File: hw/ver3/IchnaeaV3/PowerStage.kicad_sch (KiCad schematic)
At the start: 68 parts, among them Q1 BSS138, U2 LTC7871, U3 AP66200FVBW-13, U4 LM1117MP-5.0

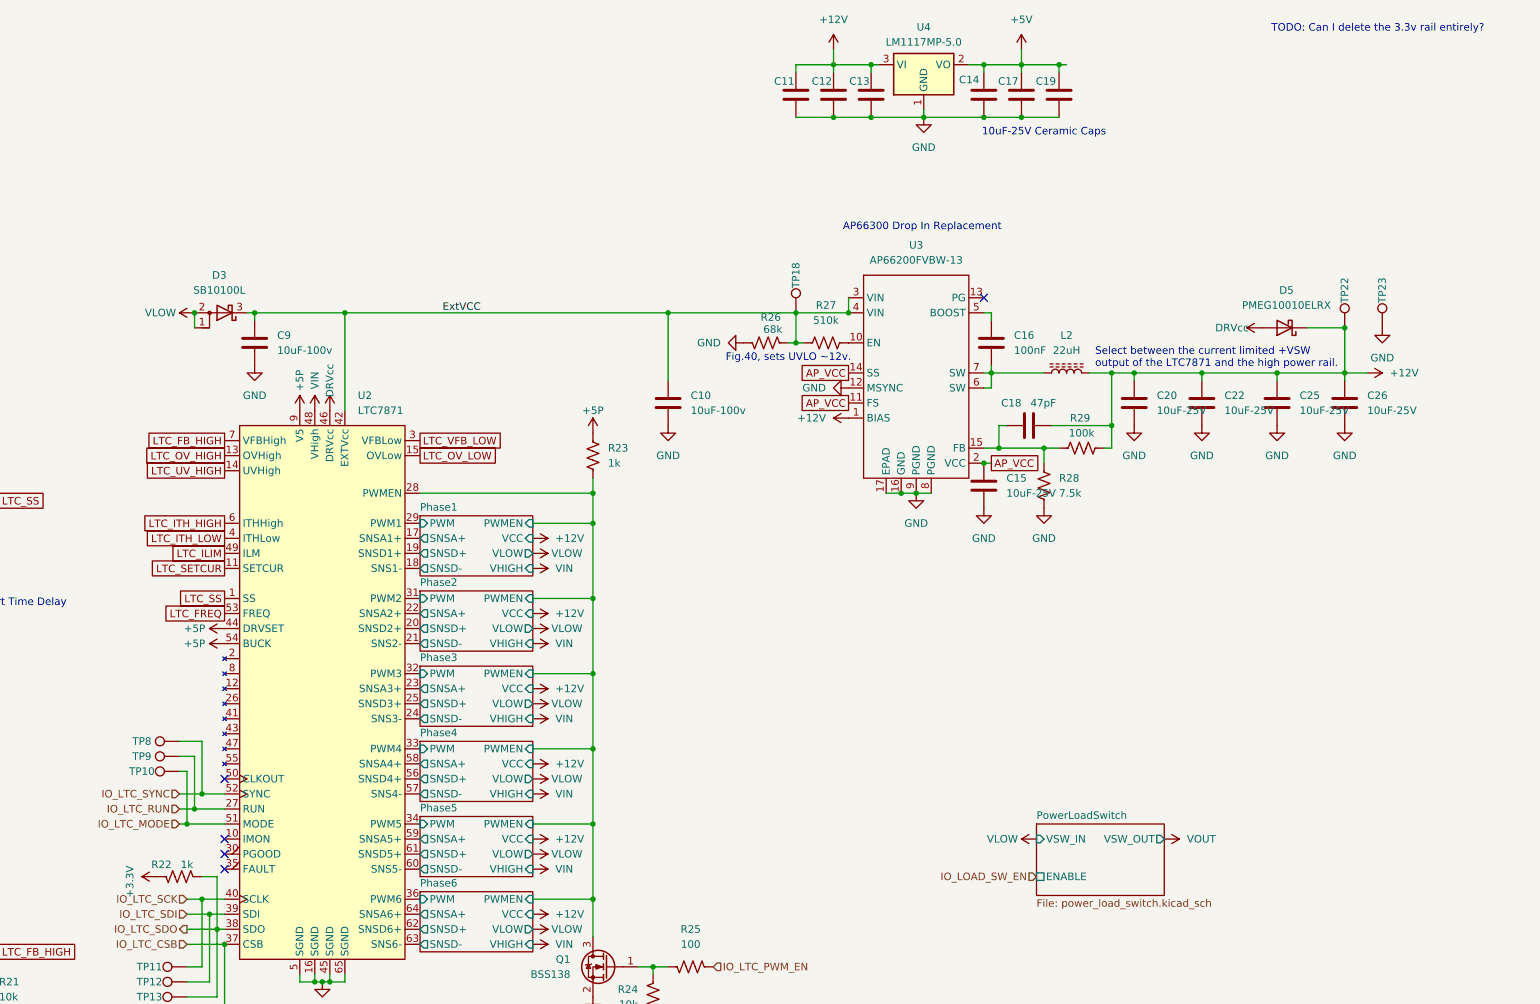
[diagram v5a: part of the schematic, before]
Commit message: Start rework of power stage layout to shorten inductive path and increase current handling
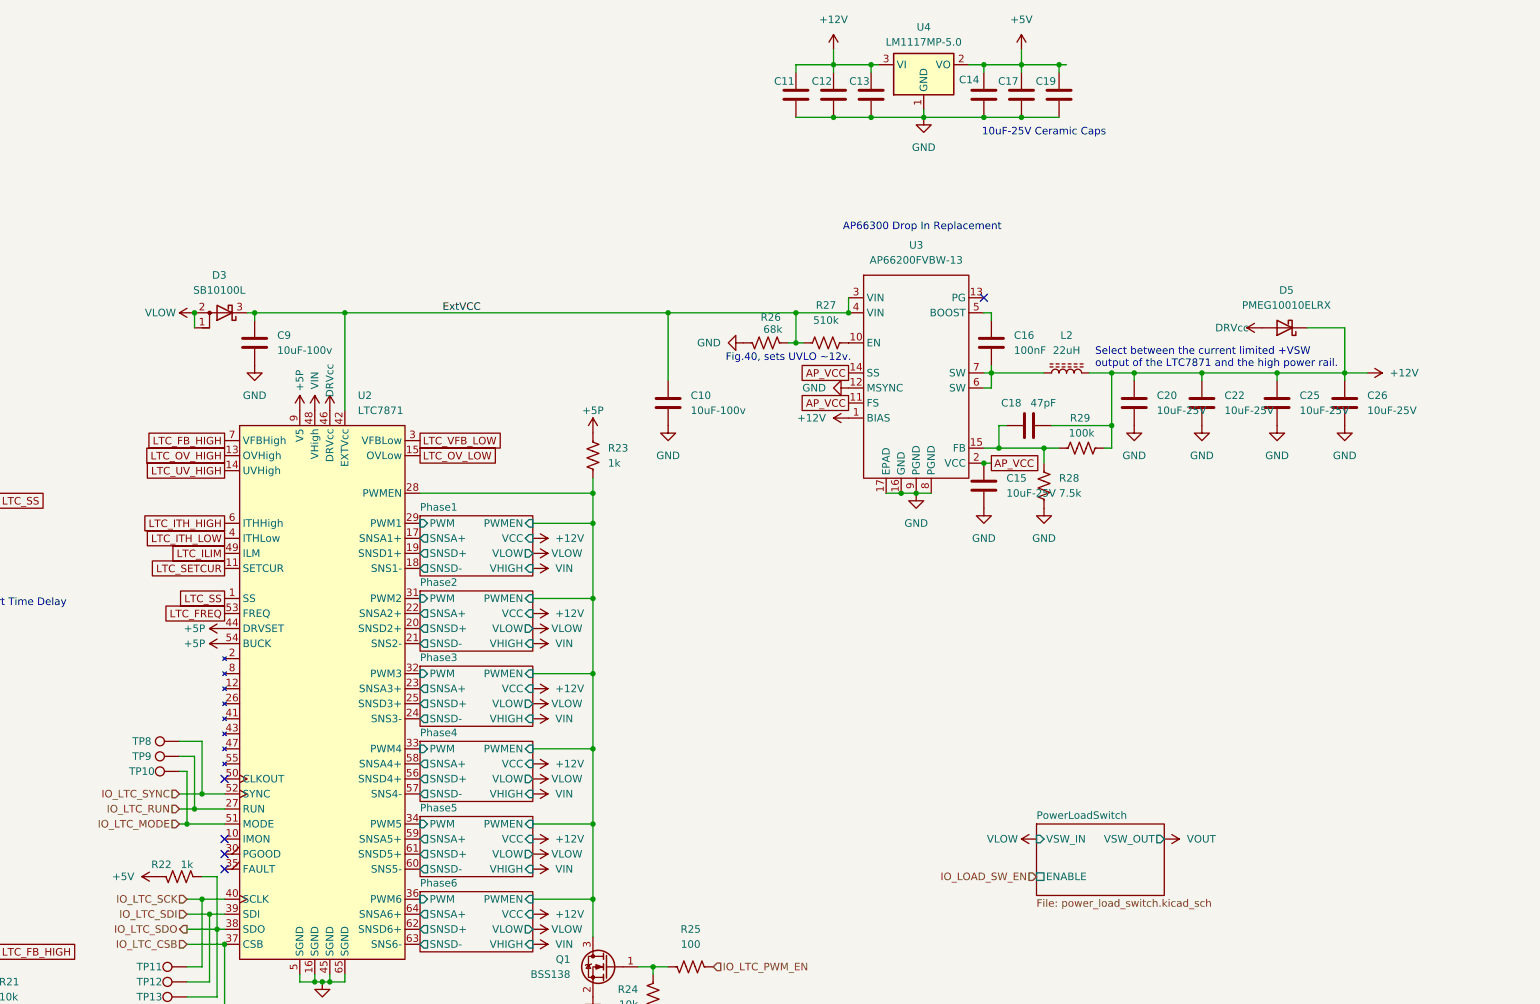
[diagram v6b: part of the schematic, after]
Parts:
- removed TP18, TP22, TP23: TestPoint, TestPoint:TestPoint_Pad_D1.0mm, symbol Connector:TestPoint
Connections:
- net +3.3V is gone; now on net +5V: R22.2
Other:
- note removed: "TODO: Can I delete the 3.3v rail entirely?"

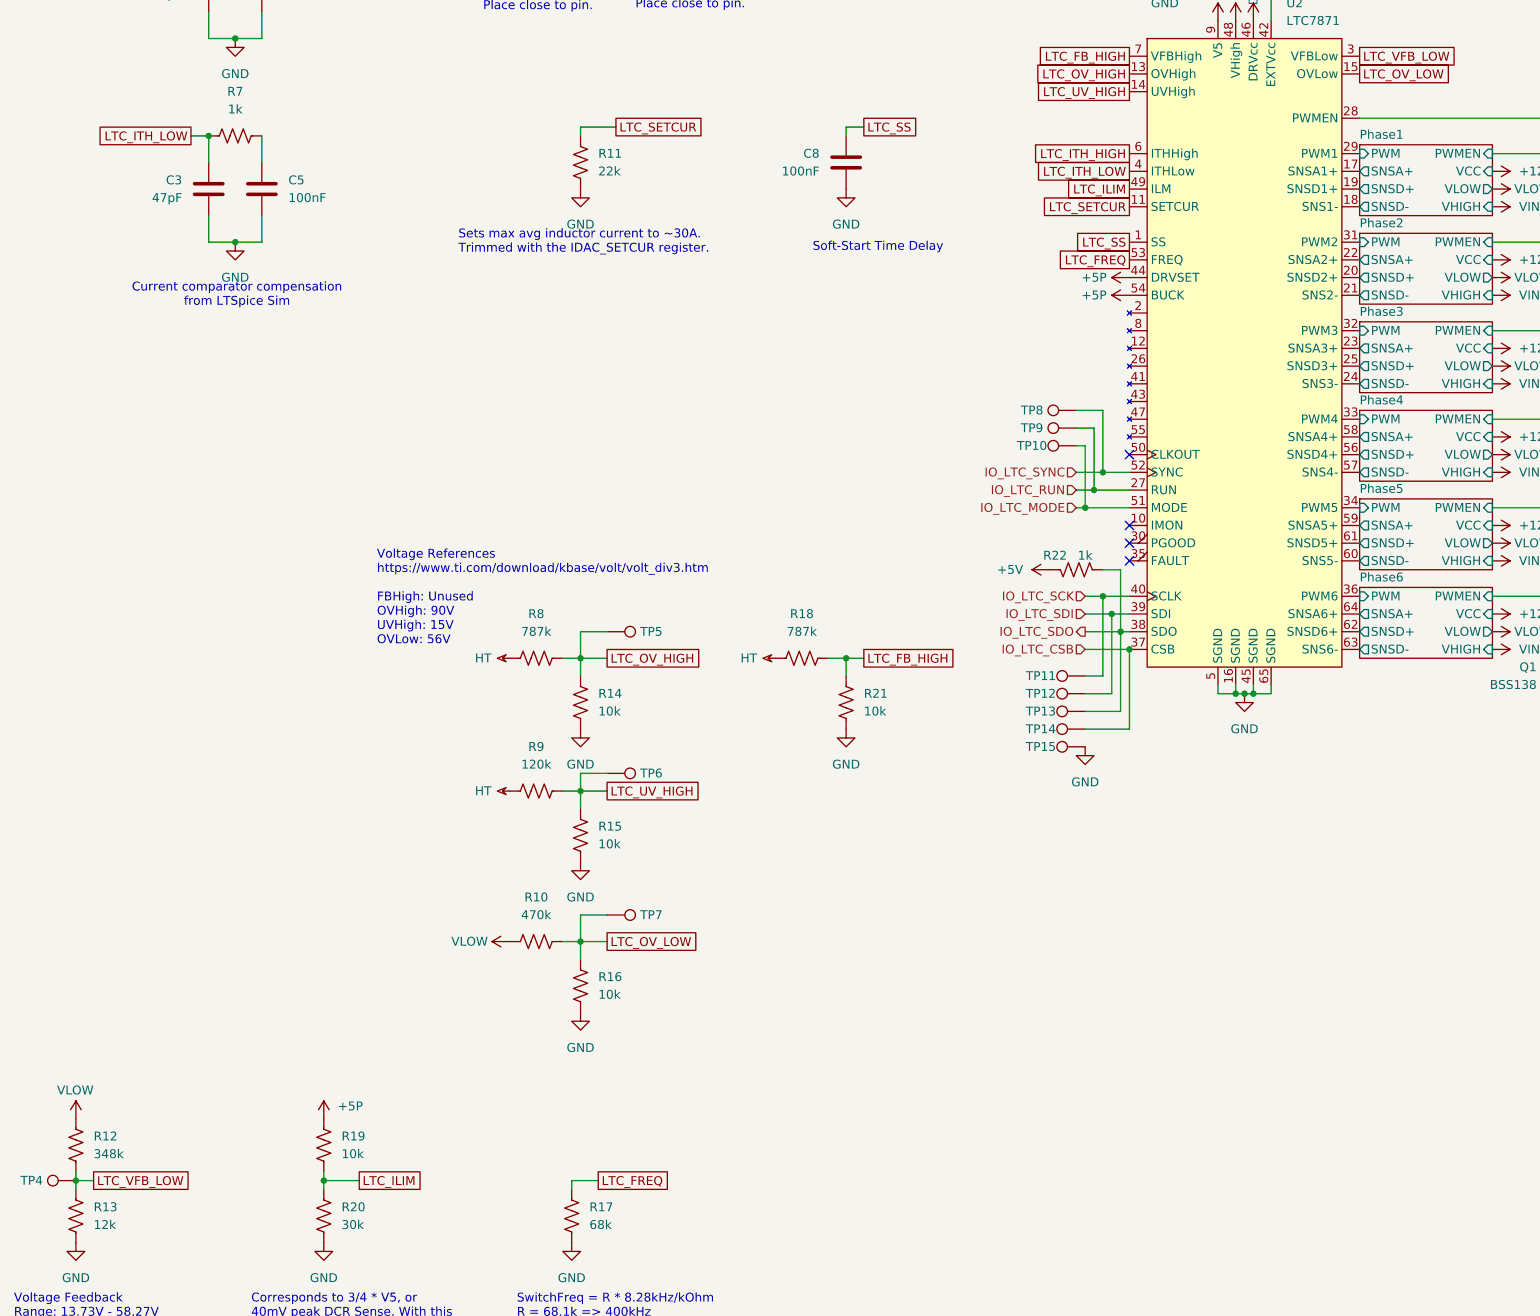
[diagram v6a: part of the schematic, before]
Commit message: Begin routing switching controller signals
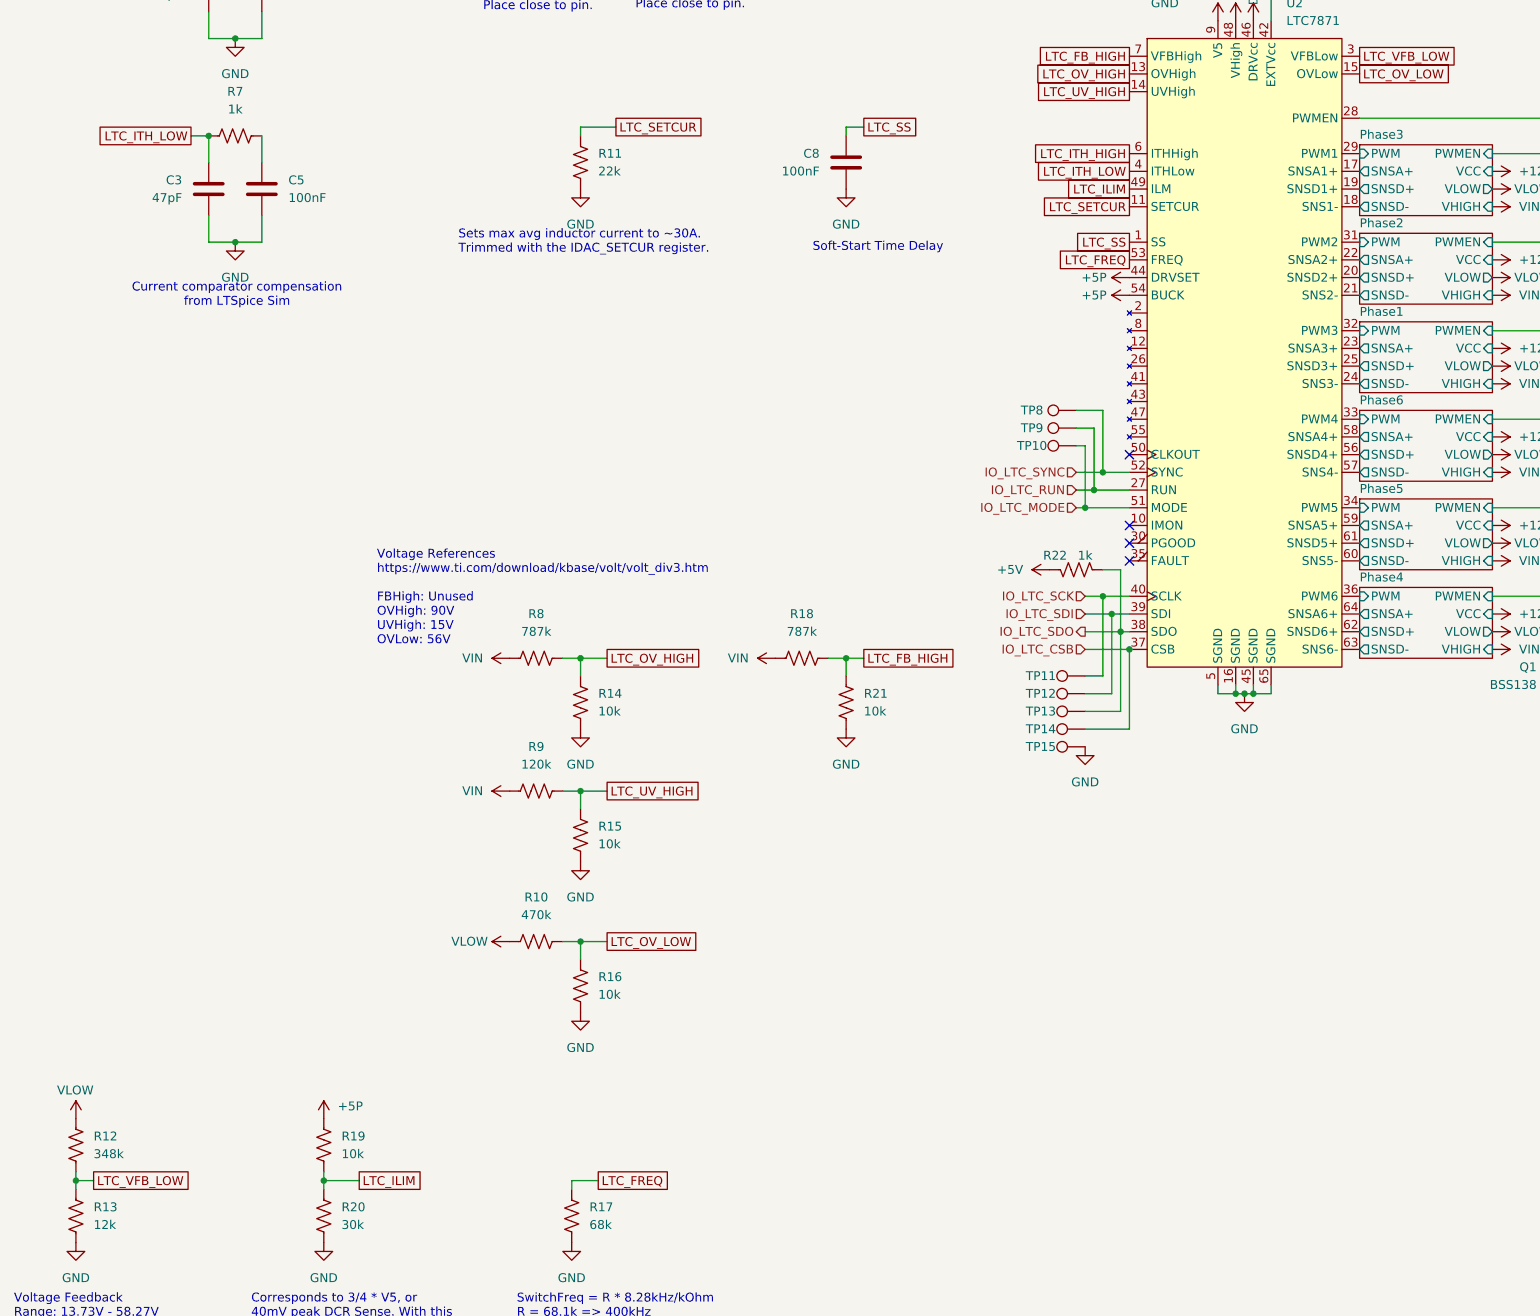
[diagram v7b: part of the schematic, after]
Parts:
- removed TP4, TP5, TP6, TP7: TestPoint, TestPoint:TestPoint_Pad_D1.0mm, symbol Connector:TestPoint
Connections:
- net HT is gone; now on net VIN: R18.1, R8.1, R9.1
- net Phase1/PWM: now also U2.32 (PWM3); no longer U2.29 (PWM1)
- net Phase1/SNSA+: now also U2.23 (SNSA3+); no longer U2.17 (SNSA1+)
- net Phase1/SNSD+: now also U2.25 (SNSD3+); no longer U2.19 (SNSD1+)
- net Phase1/SNSD-: now also U2.24 (SNS3-); no longer U2.18 (SNS1-)
- net Phase3/PWM: now also U2.29 (PWM1); no longer U2.32 (PWM3)
- net Phase3/SNSA+: now also U2.17 (SNSA1+); no longer U2.23 (SNSA3+)
- net Phase3/SNSD+: now also U2.19 (SNSD1+); no longer U2.25 (SNSD3+)
- net Phase3/SNSD-: now also U2.18 (SNS1-); no longer U2.24 (SNS3-)
- net Phase4/PWM: now also U2.36 (PWM6); no longer U2.33 (PWM4)
- net Phase4/SNSA+: now also U2.64 (SNSA6+); no longer U2.58 (SNSA4+)
- net Phase4/SNSD+: now also U2.62 (SNSD6+); no longer U2.56 (SNSD4+)
- net Phase4/SNSD-: now also U2.63 (SNS6-); no longer U2.57 (SNS4-)
- net Phase6/PWM: now also U2.33 (PWM4); no longer U2.36 (PWM6)
- net Phase6/SNSA+: now also U2.58 (SNSA4+); no longer U2.64 (SNSA6+)
- net Phase6/SNSD+: now also U2.56 (SNSD4+); no longer U2.62 (SNSD6+)
- net Phase6/SNSD-: now also U2.57 (SNS4-); no longer U2.63 (SNS6-)
